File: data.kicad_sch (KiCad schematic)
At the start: 37 parts, among them J2 USB_C_Receptacle_USB2.0, J3 Conn_01x04, SW1 SWITCH-SPST, SW2 SWITCH-SPST, U4 W25Q16JVUXIQ TR, U5 TPS22919DCKR, U6 RP2040, U7 SK6812, Y1 12MHz

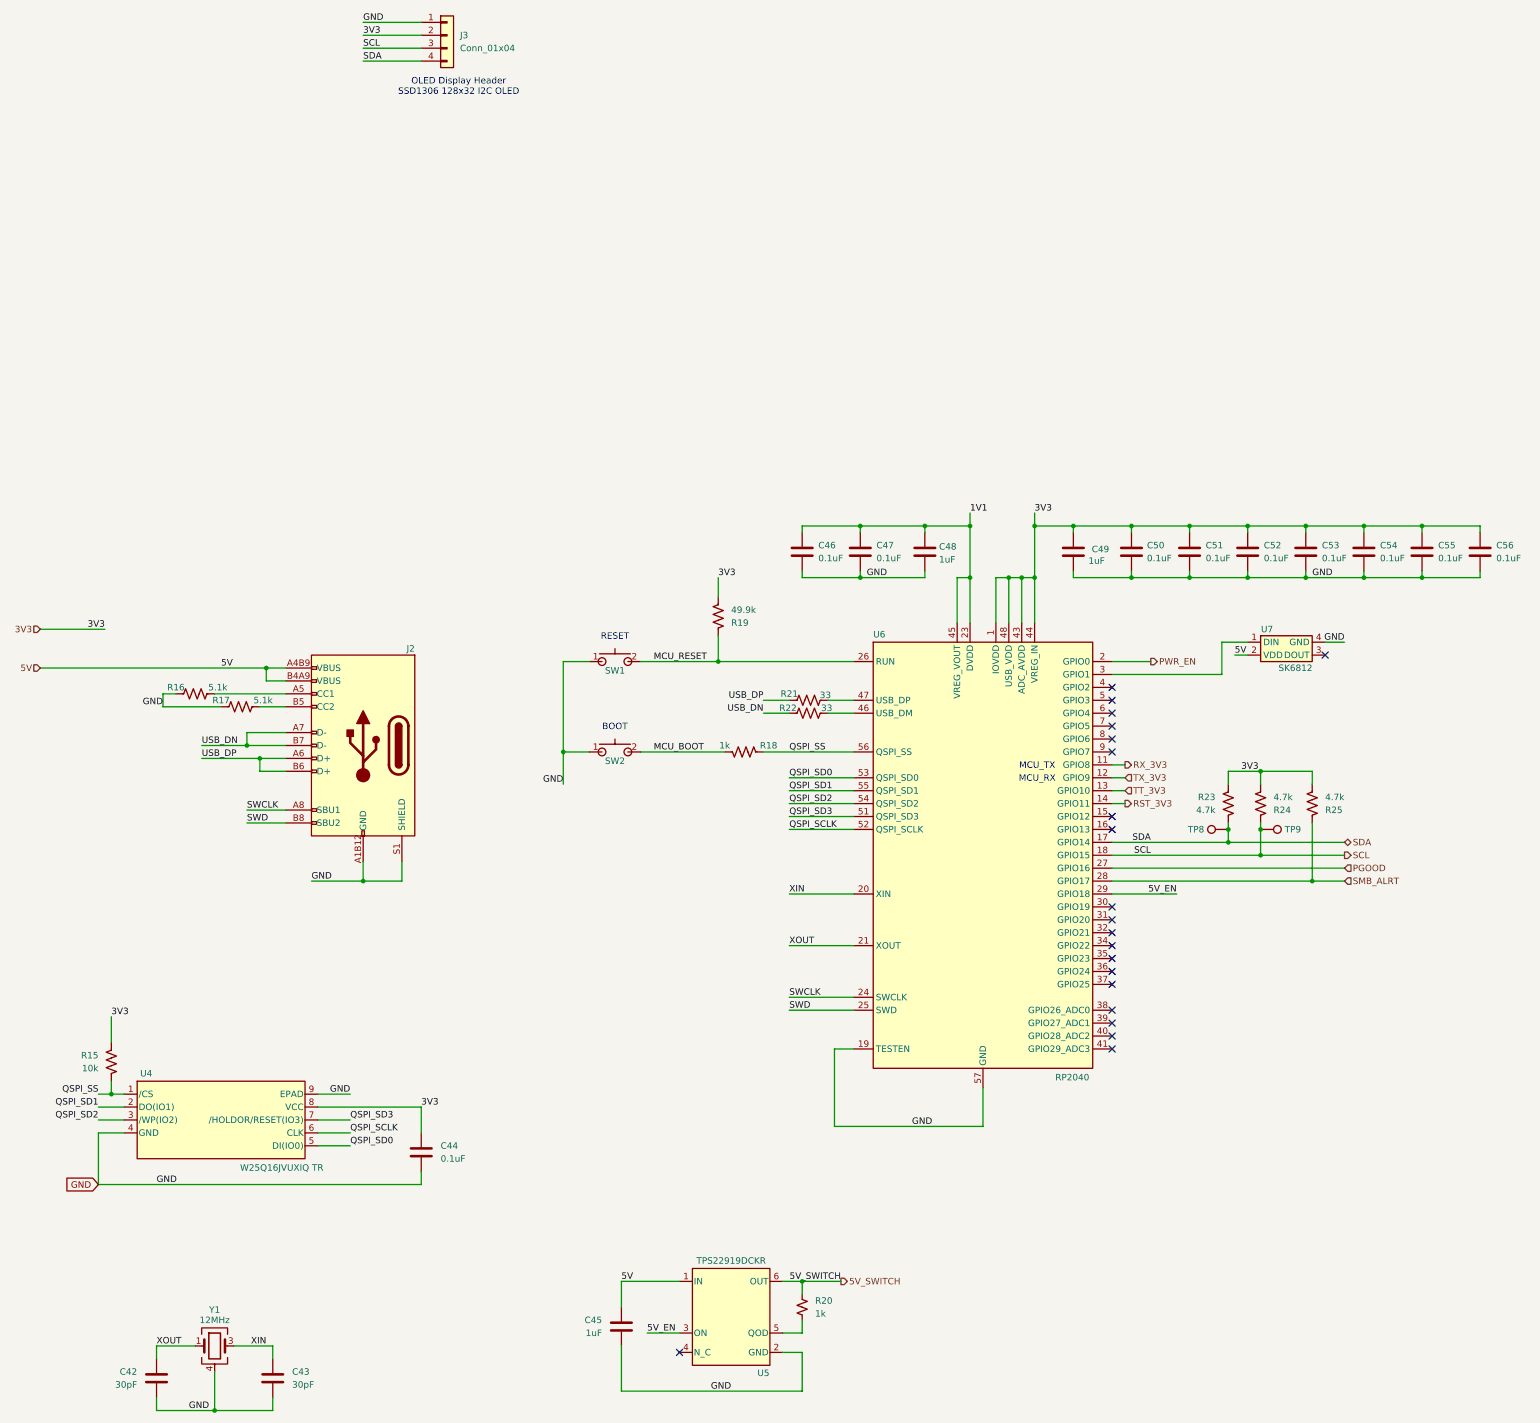
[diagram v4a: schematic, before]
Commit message: Added RP Pico W2 to schematic. Fixed Domain 1-2 level shifter pins. Added test points
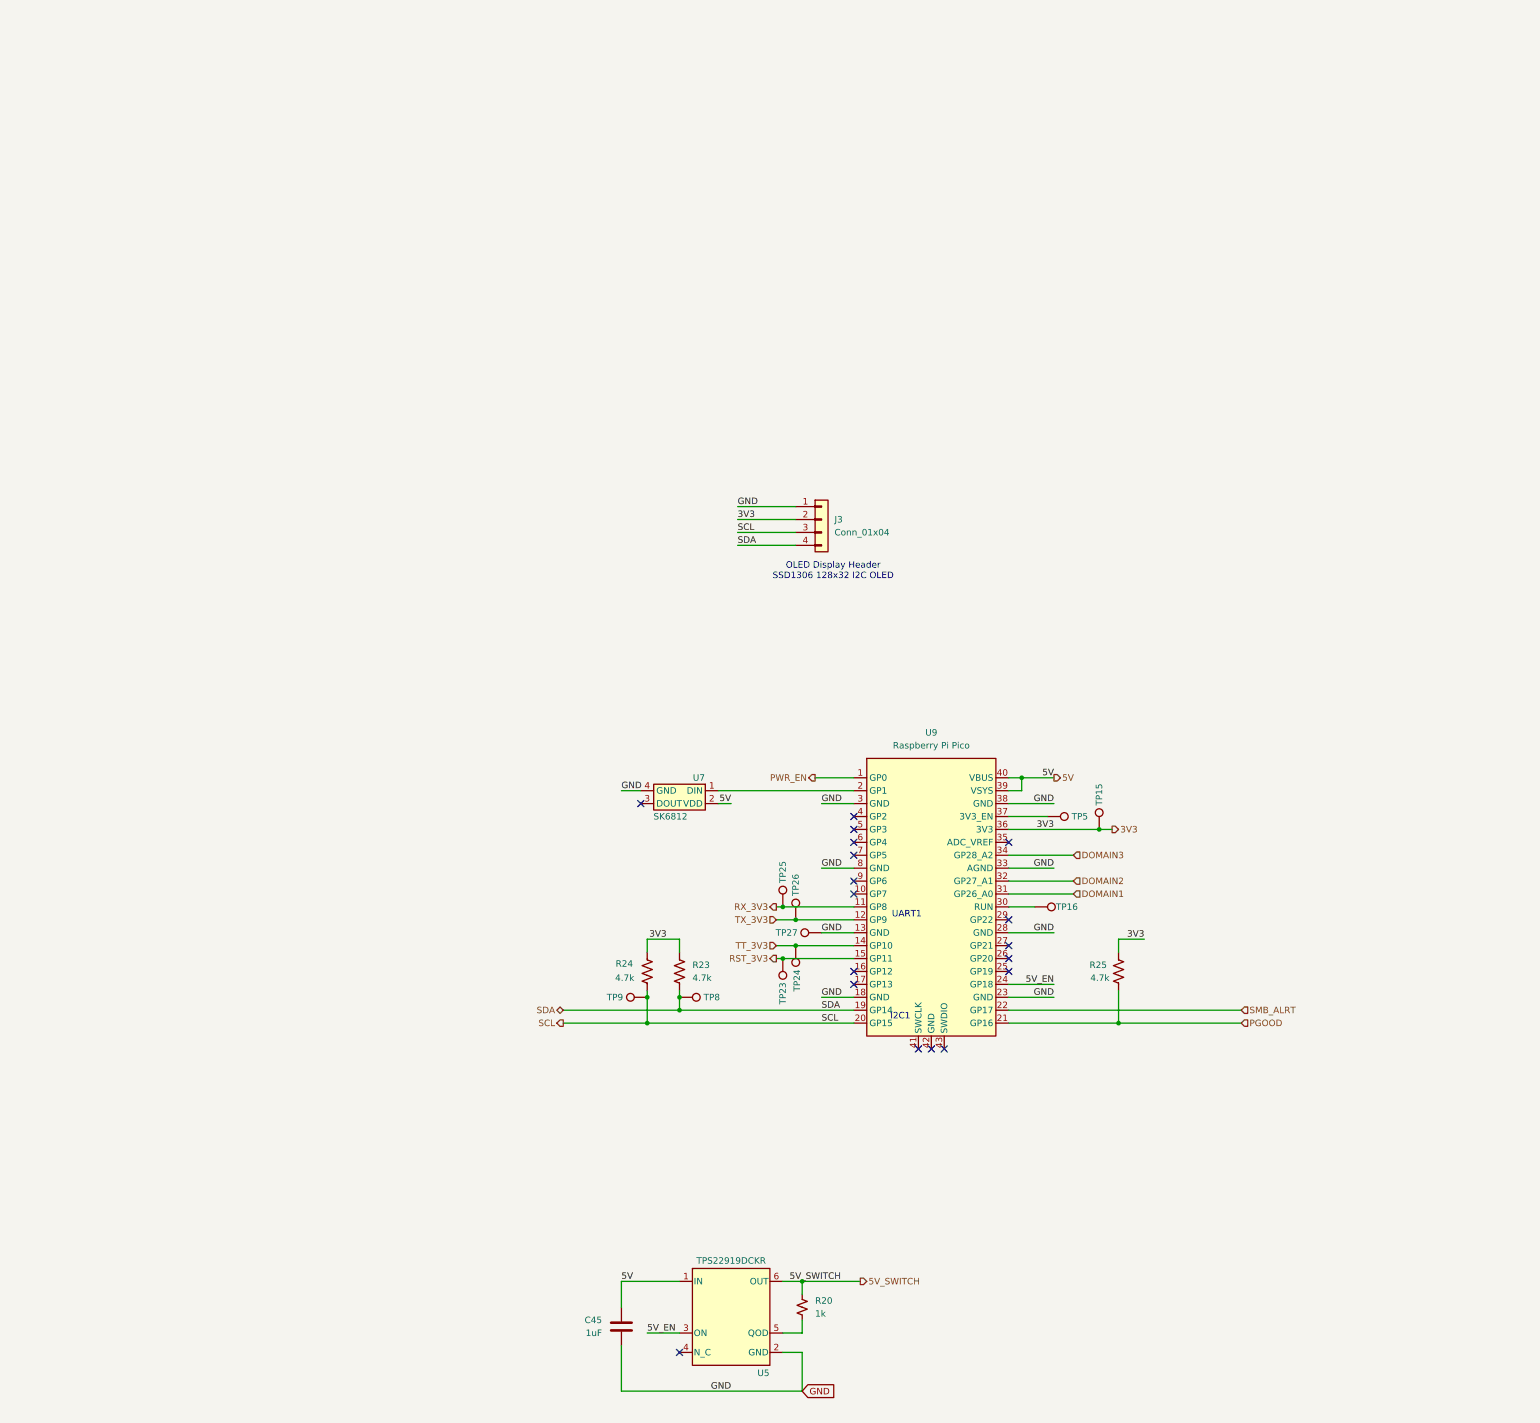
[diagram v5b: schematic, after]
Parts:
- removed C42, C43: 30pF, Capacitor_SMD:C_0402_1005Metric, symbol Device:C
- removed C44, C46, C47, C50, C51, C52, C53, C54, C55, C56: 0.1uF, Capacitor_SMD:C_0402_1005Metric, symbol Device:C
- removed C48, C49: 1uF, Capacitor_SMD:C_0402_1005Metric, symbol Device:C
- removed J2: USB_C_Receptacle_USB2.0, aditBoard:USB_C_Receptacle_GCT_USB4105-xx-A_16P_TopMnt_Horizontal, symbol aditBoard:USB_C_Receptacle_USB2.0
- removed R15: 10k, Resistor_SMD:R_0402_1005Metric, symbol Device:R_US
- removed R16, R17: 5.1k, Resistor_SMD:R_0402_1005Metric, symbol Device:R_US
- removed R18: 1k, Resistor_SMD:R_0402_1005Metric, symbol Device:R_US
- removed R19: 49.9k, Resistor_SMD:R_0402_1005Metric, symbol Device:R_US
- removed R21, R22: 33, Resistor_SMD:R_0402_1005Metric, symbol Device:R_US
- removed SW1, SW2: SWITCH-SPST, bitaxe:SW_TL3330AF130QG_EWI, symbol bitaxe:SWITCH-SPST
- removed U4: W25Q16JVUXIQ TR, emberone:USON-8_UX_2x3x0p6_WIN, symbol emberone:W25Q16JVUXIQ_TR
- removed U6: RP2040, Package_DFN_QFN:QFN-56-1EP_7x7mm_P0.4mm_EP3.2x3.2mm, symbol aditBoard:RP2040
- removed Y1: 12MHz, emberone:XTAL_ECS-120-20-33-CKM-TR3, symbol Device:Crystal_GND24_common
- added TP15, TP16, TP23, TP24, TP25, TP26, TP27, TP5: SDA, bitaxe:TestPoint_Pad_D1.0mm, symbol Connector:TestPoint
- added U9: Raspberry Pi Pico, bitaxe:RasPi_Pico_W_SMD, symbol bitaxe:Raspberry_Pi_Pico
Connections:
- net 3V3: now also TP15.1, U9.36 (3V3)
- net 5V: now also U9.39 (VSYS), U9.40 (VBUS)
- net 5V_EN: now also U9.24 (GP18)
- net GND: now also TP27.1, U9.13 (GND), U9.18 (GND), U9.23 (GND), U9.28 (GND), U9.3 (GND), U9.33 (AGND), U9.38 (GND), U9.8 (GND)
- net PGOOD: now also R25.1, U9.21 (GP16)
- net PWR_EN: now also U9.1 (GP0)
- net RST_3V3: now also TP23.1, U9.15 (GP11)
- net RX_3V3: now also TP25.1, U9.11 (GP8)
- net SCL: now also U9.20 (GP15)
- net SDA: now also U9.19 (GP14)
- net SMB_ALRT: now also U9.22 (GP17); no longer R25.1
- net TT_3V3: now also TP24.1, U9.14 (GP10)
- net TX_3V3: now also TP26.1, U9.12 (GP9)
- net at U7.1 (DIN): now also U9.2 (GP1)
- new net: TP16.1, U9.30 (RUN)
- new net: TP5.1, U9.37 (3V3_EN)
- new net DOMAIN1: U9.31 (GP26_A0)
- new net DOMAIN2: U9.32 (GP27_A1)
- new net DOMAIN3: U9.34 (GP28_A2)
- no-connect marks 21 -> 18
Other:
- note added: "I2C1"
- note added: "UART1"
- note removed: "BOOT"
- note removed: "MCU_RX"
- note removed: "MCU_TX"
- note removed: "RESET"
- moved on the sheet: J3, R23, R24, R25, TP8, TP9, U7

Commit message: switched to THT RPi Pico 2W style. Made 8mm taller.
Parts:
- TP15: value SDA -> 3V3
- TP16: value SDA -> RUN
- TP23: value SDA -> RST
- TP24: value SDA -> TT
- TP25: value SDA -> RX
- TP26: value SDA -> TX
- TP27: value SDA -> GND
- TP5: value SDA -> 3V3_EN
- U9: footprint bitaxe:RasPi_Pico_W_SMD -> bitaxe:RaspberryPi_Pico_Common_THT
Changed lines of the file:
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@@
 			)
 		)
-		(property "Value" "SDA"
+		(property "Value" "TX"
 			(at 200.6599 120.015 90)
 			(effects
@@
 			)
 		)
-		(property "Value" "SDA"
+		(property "Value" "RUN"
 			(at 252.095 124.4599 90)
 			(effects
@@
 			)
 		)
-		(property "Value" "SDA"
+		(property "Value" "TT"
 			(at 198.1201 136.525 90)
 			(effects
@@
 			)
 		)
-		(property "Value" "SDA"
+		(property "Value" "3V3_EN"
 			(at 254.635 106.6799 90)
 			(effects
@@
 			)
 		)
-		(property "Value" "SDA"
+		(property "Value" "RST"
 			(at 195.5801 139.065 90)
 			(effects
@@
 			)
 		)
-		(property "Value" "SDA"
+		(property "Value" "GND"
 			(at 198.755 127.0001 90)
 			(effects
@@
 			)
 		)
-		(property "Value" "SDA"
+		(property "Value" "3V3"
 			(at 260.3499 102.235 90)
 			(effects
@@
 			)
 		)
-		(property "Footprint" "bitaxe:RasPi_Pico_W_SMD"
+		(property "Footprint" "bitaxe:RaspberryPi_Pico_Common_THT"
 			(at 226.06 121.92 0)
 			(effects
@@
 			)
 		)
-		(property "Value" "SDA"
+		(property "Value" "RX"
 			(at 198.1199 117.475 90)
 			(effects

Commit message: lots of routing
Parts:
- removed J3: Conn_01x04, bitaxe:PinHeader_1x04_P2.54mm_Vertical_shifted, symbol Connector_Generic:Conn_01x04
- removed U7: SK6812, emberone:LED-SMD_4P-L4.0-W1.6-L, symbol athvfd:SK6812SIDE-A-RVS
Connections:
- net PWR_EN: now also U9.25 (GP19); no longer U9.1 (GP0)
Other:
- note removed: "OLED Display Header SSD1306 128x32 I2C OLED"
- moved on the sheet: R25

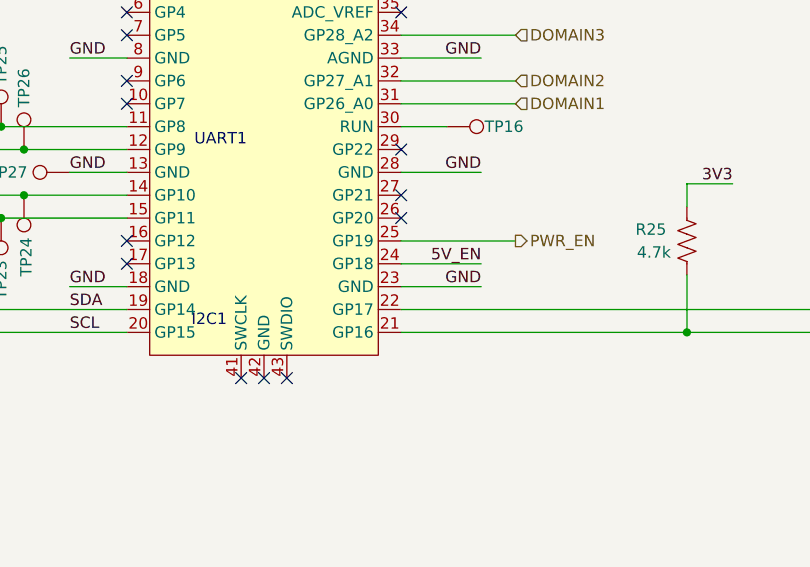
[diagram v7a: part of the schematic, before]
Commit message: Removed EMC2103, added discrete fan control, DRC pass, fixed logo.
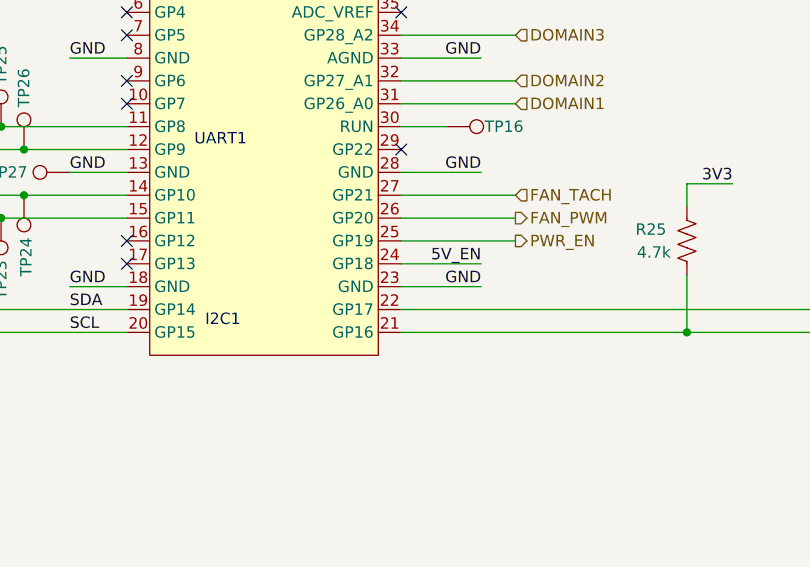
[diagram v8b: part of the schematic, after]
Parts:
- TP5: value 3V3_EN -> 3V3 EN
- U5: footprint emberone:DCK0006A_N -> bitaxe:DCK0006A_N; symbol emberone:TPS22919DCKR -> bitaxe:TPS22919DCKR
- U9: symbol bitaxe:Raspberry_Pi_Pico -> bitaxe:Raspberry_Pi_Pico_THT
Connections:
- net FAN_PWM: now reaches U9.26 (GP20)
- net FAN_TACH: now reaches U9.27 (GP21)
- no-connect marks 18 -> 13
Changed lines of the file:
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@@
 	(text "I2C1"
 		(exclude_from_sim no)
-		(at 219.964 144.78 0)
+		(at 221.488 144.78 0)
 		(effects
 			(font
@@
 	)
 	(no_connect
-		(at 228.6 151.13)
-	)
-	(no_connect
 		(at 210.82 120.65)
 	)
@@
 	)
 	(no_connect
-		(at 226.06 151.13)
-	)
-	(no_connect
 		(at 210.82 97.79)
 	)
@@
 	)
 	(no_connect
-		(at 223.52 151.13)
-	)
-	(no_connect
 		(at 241.3 125.73)
 	)
-	(no_connect
-		(at 241.3 133.35)
-	)
-	(no_connect
-		(at 241.3 130.81)
-	)
 	(wire
 		(pts
@@
 	(wire
 		(pts
+			(xy 241.3 133.35) (xy 254 133.35)
+		)
+		(stroke
+			(width 0)
+			(type default)
+		)
+	)
+	(wire
+		(pts
 			(xy 241.3 120.65) (xy 254 120.65)
 		)
@@
 		(pts
 			(xy 195.58 123.19) (xy 196.85 123.19)
+		)
+		(stroke
+			(width 0)
+			(type default)
+		)
+	)
+	(wire
+		(pts
+			(xy 241.3 130.81) (xy 254 130.81)
 		)
 		(stroke
@@
 		)
 	)
+	(hierarchical_label "FAN_PWM"
+		(shape output)
+		(at 254 133.35 0)
+		(effects
+			(font
+				(size 1.27 1.27)
+			)
+			(justify left)
+		)
+	)
 	(hierarchical_label "PWR_EN"
 		(shape output)
@@
 		(shape input)
 		(at 287.02 143.51 0)
+		(effects
+			(font
+				(size 1.27 1.27)
+			)
+			(justify left)
+		)
+	)
+	(hierarchical_label "FAN_TACH"
+		(shape input)
+		(at 254 130.81 0)
 		(effects
 			(font
@@
 	)
 	(symbol
-		(lib_id "emberone:TPS22919DCKR")
+		(lib_id "bitaxe:TPS22919DCKR")
 		(at 186.69 204.47 0)
 		(unit 1)
@@
 			)
 		)
-		(property "Footprint" "emberone:DCK0006A_N"
+		(property "Footprint" "bitaxe:DCK0006A_N"
 			(at 186.69 191.008 0)
 			(effects
@@
 			)
 		)
-		(property "Value" "3V3_EN"
+		(property "Value" "3V3 EN"
 			(at 254.635 106.6799 90)
 			(effects
@@
 	)
 	(symbol
-		(lib_id "bitaxe:Raspberry_Pi_Pico")
+		(lib_id "bitaxe:Raspberry_Pi_Pico_THT")
 		(at 226.06 121.92 0)
 		(unit 1)
@@
 		(pin "20"
 		)
-		(pin "41"
-		)
-		(pin "42"
-		)
-		(pin "43"
-		)
 		(pin "40"
